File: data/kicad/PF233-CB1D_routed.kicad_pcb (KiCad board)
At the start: 6 copper layers, 78 x 77.2 mm, 64 parts, among them M5 5 V 1.5 A switching module, U1 Pico 2 W

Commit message: KiCad schematics for 7 boards; fix the trigger input (digital Hall switch, 47k pull-up)
- sch_export.py: .kicad_sch for CB1D, LB1, AB1A, AB1B, PB1R, PM1, HB1 from
  the netlists (box symbol per part, net label on every pin); sch_check
  rebuilds the nets from each file and matches the netlist exactly (7/7).
  Not opened in KiCad; no KiCad ERC. `make sch`, run from verify-full.
- trigger_check.py: traces HB1 HS1 -> JH.3 -> W013 -> CB1D JTR.3 -> TRIG_IN
  -> Pico pin 7, checks sensor type vs GPIO type, levels, time constant,
  dial ladder at the ADC, joystick switch, boost stress rows.
- Defects found: the linear SS49E fed a digital-only GPIO (undefined state
  at rest), and the low level through 2 kohm into a 10k pull-up was 0.88 V
  (VIL 0.8). HB1 now uses a generic digital open-drain Hall switch (part and
  pinout unverified) and CB1D RP1 is 47k: low 0.52 V, 0.47 ms. RP1 is the
  same 0603, so CB1D copper and Gerbers are unchanged (only the value text).
- Joystick push switch does not reach the head (warn, OPEN_ITEMS 16);
  BOM_MASTER.csv cannot be regenerated (OPEN_ITEMS 17).
- make pcb-hb1; regress: schematics round trip and handle inputs.

Co-Authored-By: Claude Opus 5.5 <noreply@anthropic.com>
Claude-Session: https://claude.ai/code/session_01SK9nuqTzvCJwnmscD6XRZs
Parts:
- RP1: value 10k -> 47k
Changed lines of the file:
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@@
   (footprint "Resistor_SMD:R_0603_1608Metric" (layer "F.Cu") (at 130.5000 82.0000)
     (property "Reference" "RP1" (at 0 -2.5 0) (layer "F.SilkS") (effects (font (size 0.8 0.8) (thickness 0.12))))
-    (property "Value" "10k" (at 0 2.5 0) (layer "F.Fab") (effects (font (size 0.8 0.8) (thickness 0.12))))
+    (property "Value" "47k" (at 0 2.5 0) (layer "F.Fab") (effects (font (size 0.8 0.8) (thickness 0.12))))
     (attr smd)
     (pad "1" smd roundrect (at -0.825 0.000) (size 0.800 0.950) (layers "F.Cu" "F.Paste" "F.Mask") (net 42 "TRIG_IN"))

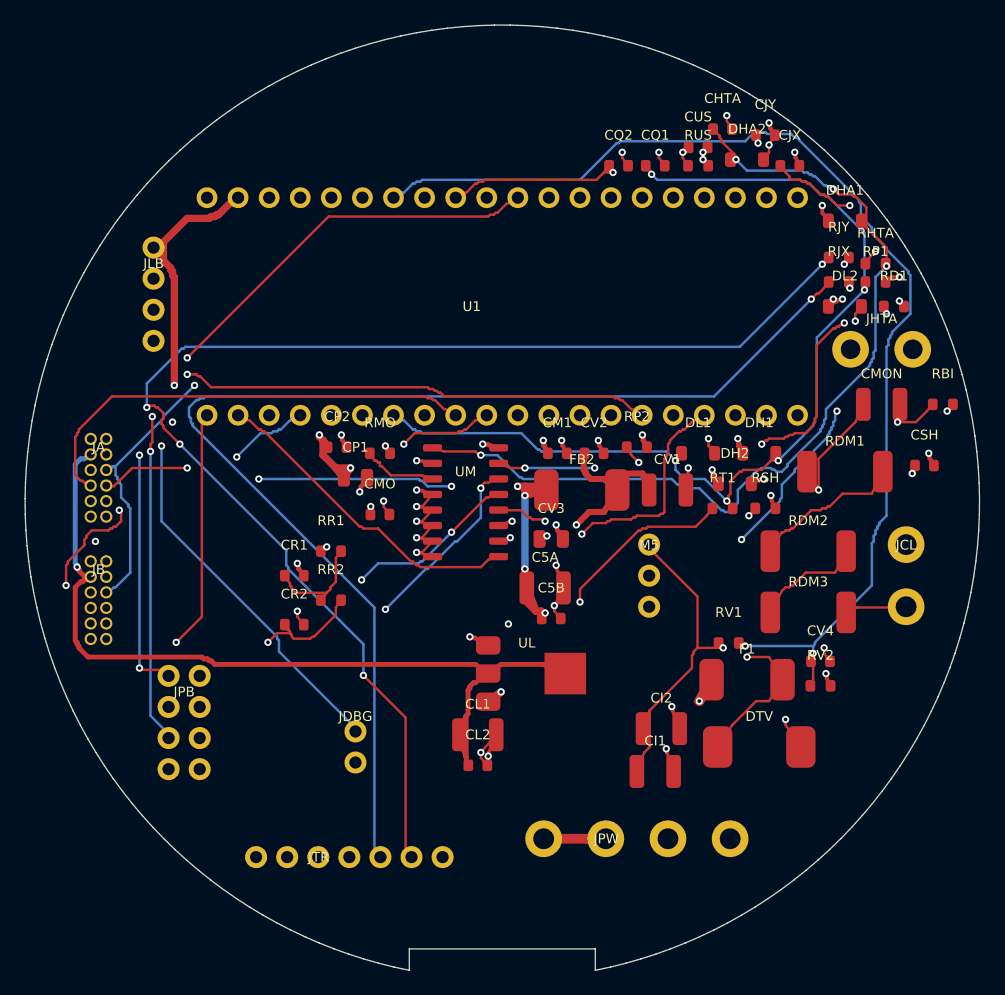
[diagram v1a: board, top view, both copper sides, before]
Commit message: External KiCad 9 DRC, CB1D-B revision, HV plane keep-out, router/export fixes (step 1 of the transmit-region sign-off)
- KiCad 9.0.9 installed; kicad_drc.py (zone fill, design rules, automatic negative control), dru_gen.py (last rule wins), make kicad-drc
- CB1D-B: MONO 460 V tap and joystick inputs removed, parts kept inside the rib annulus; 58 parts, 41/41 nets, 1669 mm, 101 vias
- CB1D and LB1: KiCad 0 errors / 0 unconnected; independent DRC 0/0; head cross-check 0 fail; wiring audit clean
- gerber_out: 1.0 mm plane keep-out for HV pads and vias (gerber_hv_check.py, control proves the old writer failed 8/8)
- route_fix: nearest-pad stubs, circle test for round pads, duplicate vias; kicad_inject: template zones no longer kept
- new Gerbers CB1D_B and LB1_v4; CB1D_v2 and LB1_v3_stubbed marked superseded
- regress 39 pass; CORRECTIONS, DESIGN_STATE, OPEN_ITEMS 20/23/24, ASSUMPTIONS 30

Not done: PB1R routing, TXJ1 edge clearance, SB1R annular rings, CAM viewer, datasheets, bench test.

Co-Authored-By: Claude Sonnet 5.5 <noreply@anthropic.com>
Claude-Session: https://claude.ai/code/session_01T7iU5pGiBfkKRBbe2JcTJx
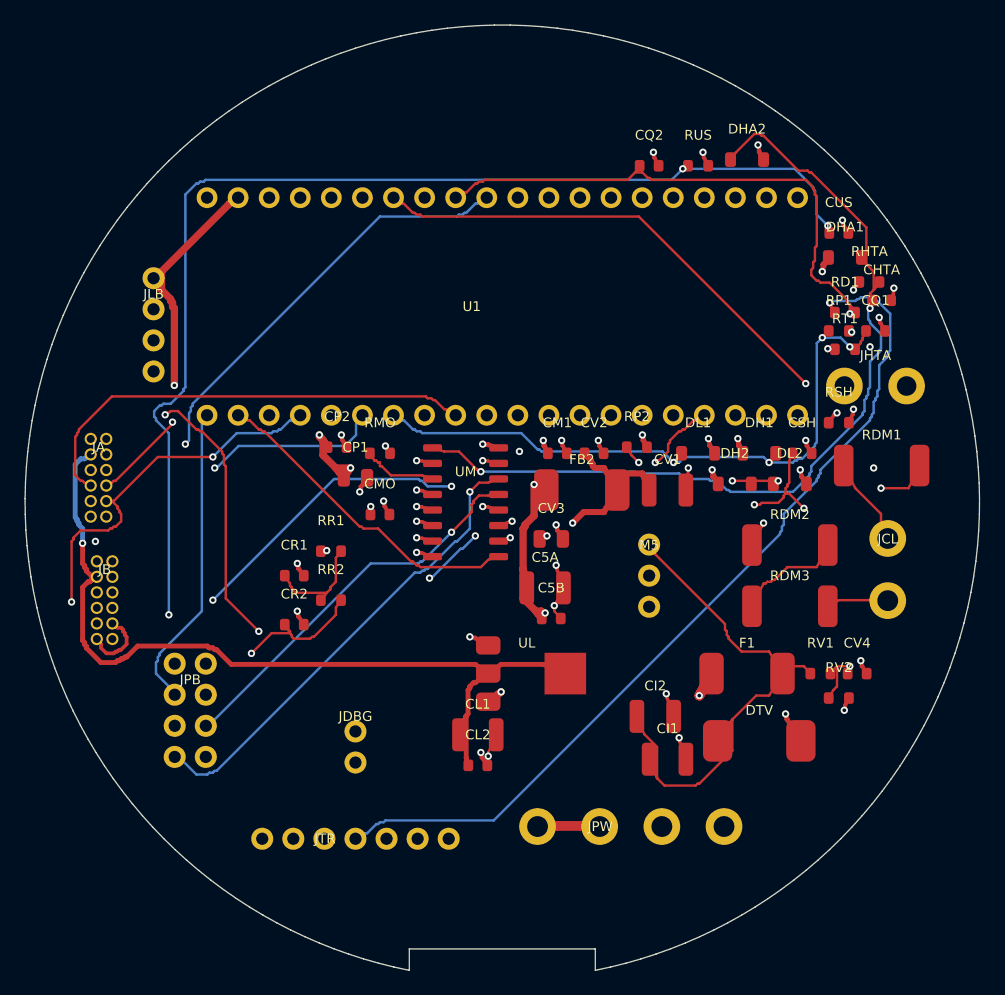
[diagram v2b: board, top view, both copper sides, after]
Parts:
- removed CJX, CJY: 10n, Capacitor_SMD:C_0603_1608Metric
- removed CMON: 100n 630V, Capacitor_SMD:C_1210_3225Metric
- removed RBI: 100k, Resistor_SMD:R_0603_1608Metric
- removed RJX, RJY: 1k, Resistor_SMD:R_0603_1608Metric
- moved CQ1 22.5 mm to (130.5, 86.0)
- moved CHTA 19.1 mm to (131.0, 83.5)
- moved RT1 16.4 mm to (128.0, 87.5)
- moved DL2 15.2 mm to (123.5, 98.5)
- moved CUS 13.5 mm to (127.5, 78.0)
- moved CSH 10.0 mm to (124.5, 96.0)
- moved RSH 9.22 mm to (127.5, 93.5)
- moved RV1 7.91 mm to (126.0, 114.0)
- moved RP1 5.00 mm to (127.5, 86.0)
- moved RD1 4.03 mm to (128.0, 84.5)
- moved CV4 3.16 mm to (129.0, 114.0)
- moved JHTA 3.04 mm to (130.5, 90.5)
- moved RDM1 3.04 mm to (131.0, 97.0)
- moved DHA1 3.00 mm to (128.0, 80.0)
- moved CQ2 2.50 mm to (112.0, 72.5)
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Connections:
- JB pad 10: MONO_IN -> VCM_OUT
- JTR pad 5: JOY_X -> JTR5_NC
- JTR pad 6: JOY_Y -> JTR6_NC
- UM pad 12: JOY_YF -> GND
- UM pad 15: JOY_XF -> GND
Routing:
- net JOY_Y: track 108.2 -> 0.00 mm, vias 4 -> 0
- net JOY_X: track 98.8 -> 0.00 mm, vias 1 -> 0
- net MONO_IN: track 79.5 -> 0.00 mm, vias 2 -> 0
- net VCM_OUT: track 79.8 -> 5.81 mm, vias 1 -> 0
- net JOY_YF: track 61.0 -> 0.00 mm, vias 3 -> 0
- net JOY_XF: track 56.4 -> 0.00 mm, vias 6 -> 0
- net TRIG_EXT: track 43.8 -> 79.2 mm
- net TRIG_IN: track 86.0 -> 57.5 mm, vias 5 -> 4
- net VBUS_SENSE: track 95.2 -> 73.5 mm, vias 2 -> 3
- net FAULT1_N: track 69.0 -> 54.9 mm
- net COIL_B: track 21.2 -> 7.16 mm, vias 1 -> 0
- net UMB_SHLD: track 87.7 -> 99.1 mm
- net GND: track 92.6 -> 101.4 mm
- net DIAL_EXT: track 66.6 -> 74.2 mm, vias 3 -> 1
- net DM1: track 12.5 -> 19.2 mm, vias 0 -> 2
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- removed copper zone on In2.Cu, net VBUS

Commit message: Step 2: CB1D options, SB1R via drill, TXJ1 pads, fab-floor rules, finishes (KiCad 9: 5 boards, 0 errors / 0 unconnected)
- SB1R: via drill 0.4 mm (was 0.8 = no annular ring in the KiCad files and the PTH drill files); QB transfer nets QB_T1/QB_T2; Gerbers SB1R_QA_v2 / SB1R_QB_v2, old marked superseded; sbq sims unchanged (0 numbers moved)
- TXJ1: AWG12 pads 3.8 mm (edge distance 0.6 mm); Gerbers TXJ1_v2
- CB1D: RJB10 0R fitted on JB.10, RJ5/RJ6 DNP grounds for JTR.5/.6 (61 parts, 44/44 nets); Gerbers CB1D_B2; wiring alias JB10_VCM
- dru_gen: conservative Advanced Circuits / TTM floor (UNVERIFIED), SB1R keys; no ENIG near the coil/receivers (immersion silver / HASL); docs/design/FAB_RULES.md
- make kicad-drc covers CB1D, LB1, TXJ1, SB1R-QA/QB; regress 42 pass; CORRECTIONS, DESIGN_STATE, OPEN_ITEMS 23/25-27, ASSUMPTIONS 31

Co-Authored-By: Claude Sonnet 5.5 <noreply@anthropic.com>
Claude-Session: https://claude.ai/code/session_01T7iU5pGiBfkKRBbe2JcTJx
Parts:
- added RJ5: 0R DNP, Resistor_SMD:R_0603_1608Metric, F.Cu at (92.0, 124.0)
- added RJ6: 0R DNP, Resistor_SMD:R_0603_1608Metric, F.Cu at (92.0, 121.0)
- added RJB10: 0R, Resistor_SMD:R_0603_1608Metric, F.Cu at (105.0, 131.0)
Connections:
- JB pad 10: VCM_OUT -> JB10_VCM
- JTR pad 5: JTR5_NC -> JTR5_OPT
- JTR pad 6: JTR6_NC -> JTR6_OPT
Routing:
- net JB10_VCM: track 0.00 -> 45.1 mm, vias 0 -> 1
- net VCM_OUT: track 5.81 -> 48.0 mm
- net JTR6_OPT: track 0.00 -> 7.89 mm, vias 0 -> 1
- net JTR5_OPT: track 0.00 -> 4.47 mm, vias 0 -> 1
- net GND: track 101.4 -> 105.9 mm, vias 37 -> 39
- net BLANK: track 33.7 -> 38.0 mm
- net +3V3D: track 71.8 -> 68.7 mm
- net SHIELD: track 57.2 -> 58.4 mm, vias 3 -> 2
- net TRIG_EXT: track 79.2 -> 79.8 mm
- net CS: track 34.2 -> 34.4 mm, vias 1 -> 2
- net SDOB1: vias 0 -> 1

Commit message: Step 5: datasheets and fabricator sheets (vendor-derived floor, verified parts, PB1R 9-can bank, Gerber edge read-back)
- Fab floor from AdvancedPCB / TTM pages (docs/design/FAB_RULES_VERIFIED.md, U-FAB-RULES closed): clearance 0.16,
  component-PTH ring 0.18 / hole 0.46, drill-copper 0.26, drill-drill 0.41, every rule (severity error).
  CB1D JA/JB and HB2 TO-92 pads 1.02 mm; route_fix merges close same-net vias (CB1D, LB1).
- Parts from manufacturer PDFs (docs/design/DATASHEET_LOG.md): PB1R bulk 9 x Panasonic EEHZC1H101P
  (the 150 uF / 50 V polymer-Ta was not found; bank stays 900 uF, on-time table unchanged), PB1R re-placed
  with the Kelvin/comparator cluster pinned (pulse path 4.9 mohm, spike 7.5 V, ground ref 15.5 mV unchanged);
  SMCJ30A (SMCJ33A clamps 53.3 V > 50 V parts), Si4401FDY, BZT52C15, Bourns SF-1206S500-2 (new 1206 land),
  DRV5023BIQLPG, CRCW2512 500 V, OPA2365/OPA2211/LM393/CD74HC4051 checked. ES3J 600 V kept as a WATCH.
- U-DS-PARTS split into groups; open: TXDRIVE, OKI, PACK, BAV199, HVTERM. U-COLD-BOOTSTRAP closed.
- Controls retargeted to fixture folders (12/12). Netlist date fixed (data changed daily).
- Gerber planes from gerber_out.py ran into the notch and to 0.1 mm of the edge since r1 (found by the
  independent review): fixed, and gerber_edge_check.py reads every copper layer back.
- New Gerber sets CB1D_B3, LB1_v5, PB1R_v2; old sets marked SUPERSEDED.
- Findings for the owner: aluminium cans ~0.5 x a 1 g nugget (OPEN_ITEMS 34), OPA2365 capacitive load (30),
  OPA2211 input range on 5 V (31), Hall magnet spread (32).
- Strict regress 55 PASS / 0 FAIL / 0 SKIP; sign-off 44 PASS / 0 FAIL / 0 SKIP / 19 UNVERIFIED.

Co-Authored-By: Claude Opus 5.5 <noreply@anthropic.com>
Claude-Session: https://claude.ai/code/session_015VKhZtgEAWnezB2NDY75VV
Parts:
- DTV: value SMCJ33A -> SMCJ30A
- F1: footprint Fuse:Fuse_1812_4532Metric -> Fuse:Fuse_1206_3216Metric
- moved F1 11.0 mm to (124.5, 124.0)
- moved RV2 5.59 mm to (122.0, 115.0)
- moved RV1 4.47 mm to (122.0, 112.0)
- moved CV4 4.00 mm to (125.0, 114.0)
- moved CI2 1.00 mm to (113.5, 117.5)
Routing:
- net VBUS: track 47.0 -> 54.3 mm, vias 0 -> 2
- net VBUS_IN: track 26.7 -> 23.8 mm, vias 1 -> 0
- net VBUS_SENSE: track 73.5 -> 75.9 mm
- net GND: track 105.9 -> 106.4 mm, vias 39 -> 38
